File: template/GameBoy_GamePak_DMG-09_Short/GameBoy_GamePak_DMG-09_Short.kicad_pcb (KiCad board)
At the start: 2 copper layers, 51 x 48.1 mm, 1 part, among them J1 GameBoy_GamePak_DMG-09

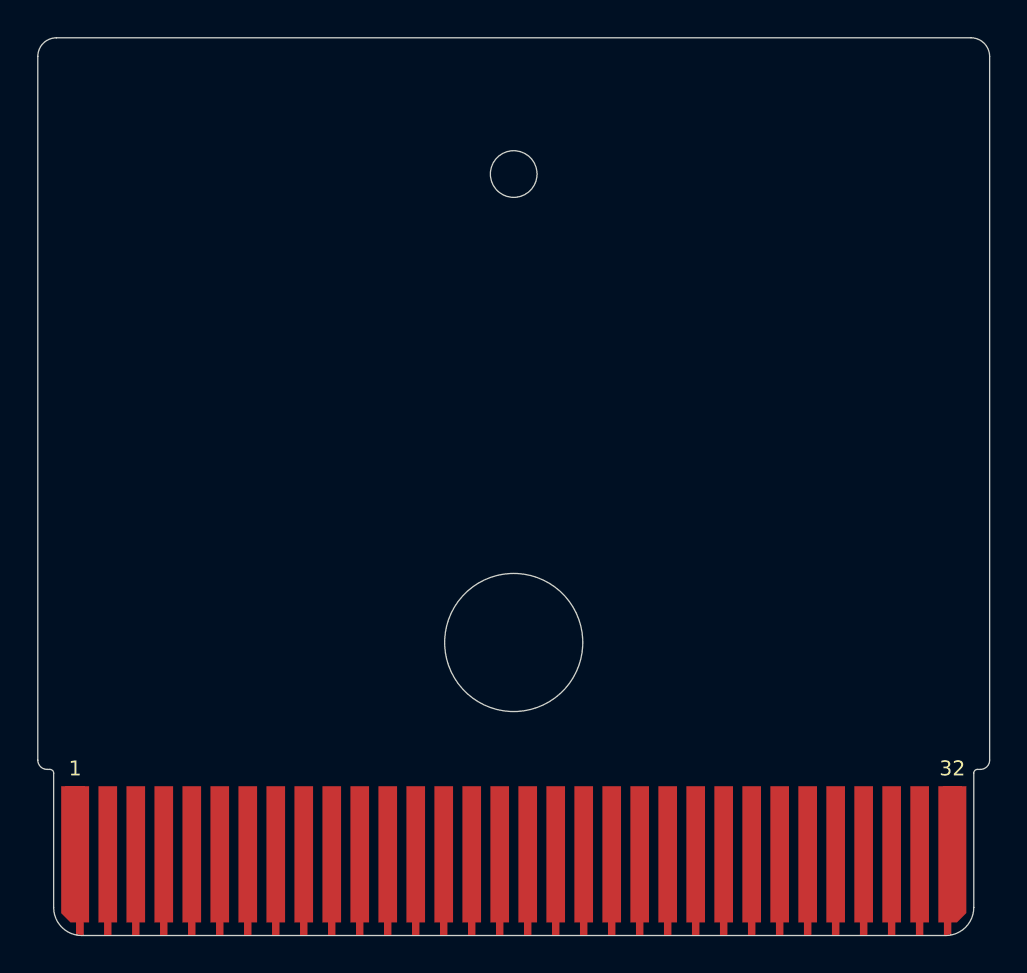
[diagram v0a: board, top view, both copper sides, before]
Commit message: Update all files to KiCAD 6.x format
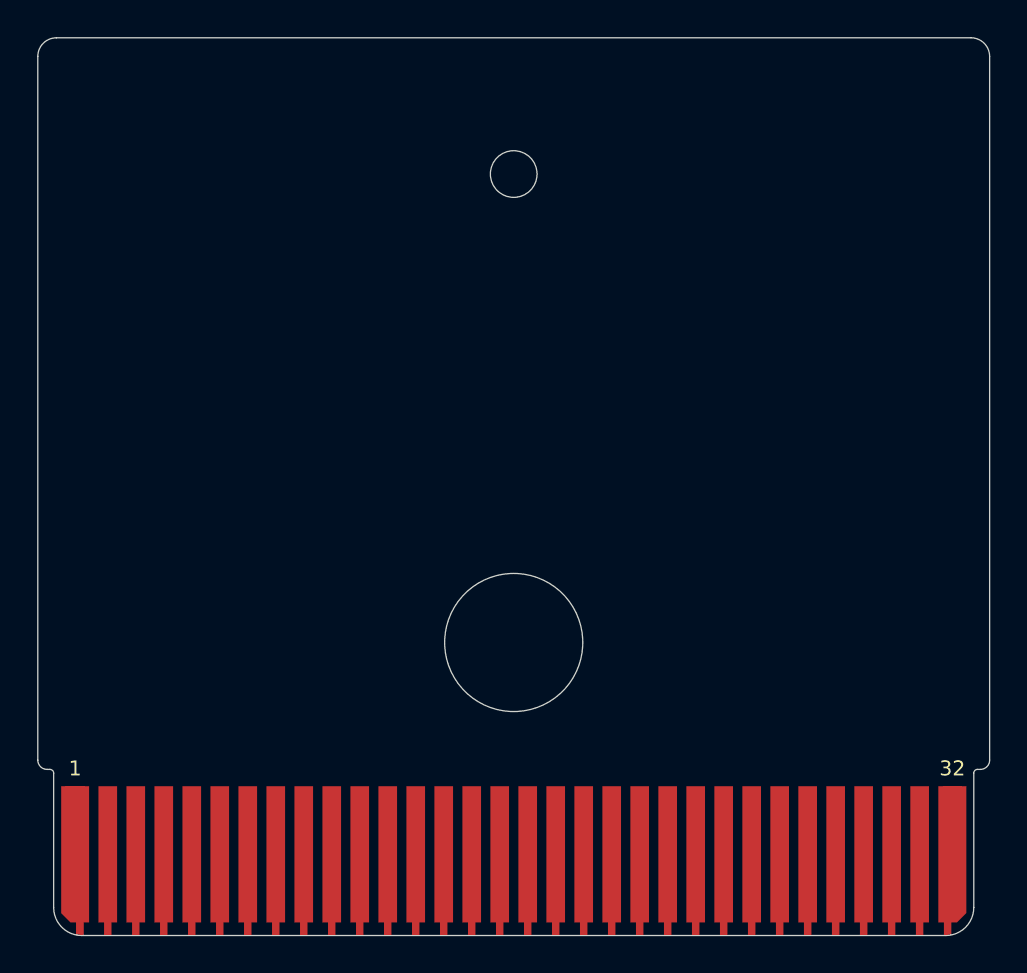
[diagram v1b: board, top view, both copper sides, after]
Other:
- outline, holes or cut-outs redrawn
- net class Default removed
